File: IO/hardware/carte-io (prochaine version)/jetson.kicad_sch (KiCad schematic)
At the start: 8 parts, among them J1 Multiplex MPX 6, J23 Conn_02x20_Odd_Even, J26 114020164

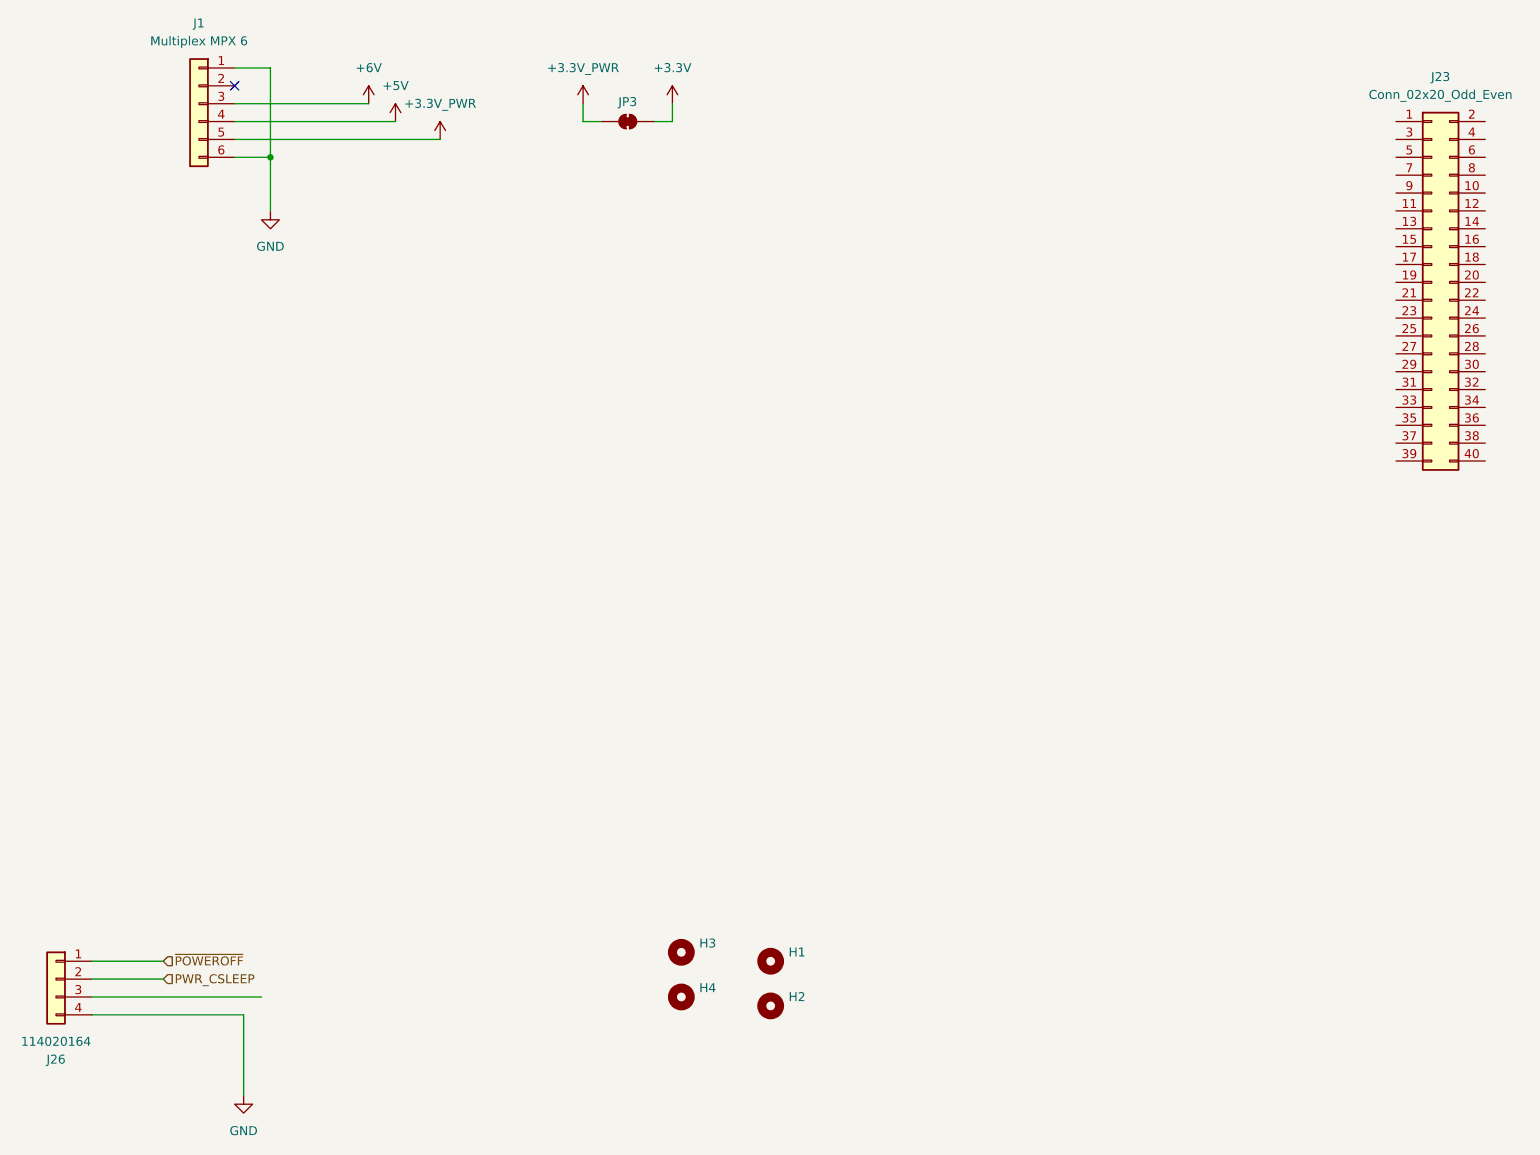
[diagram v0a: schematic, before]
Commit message: Recuperation de la carte IO perdue lors de la suppression des 3 derniers commit
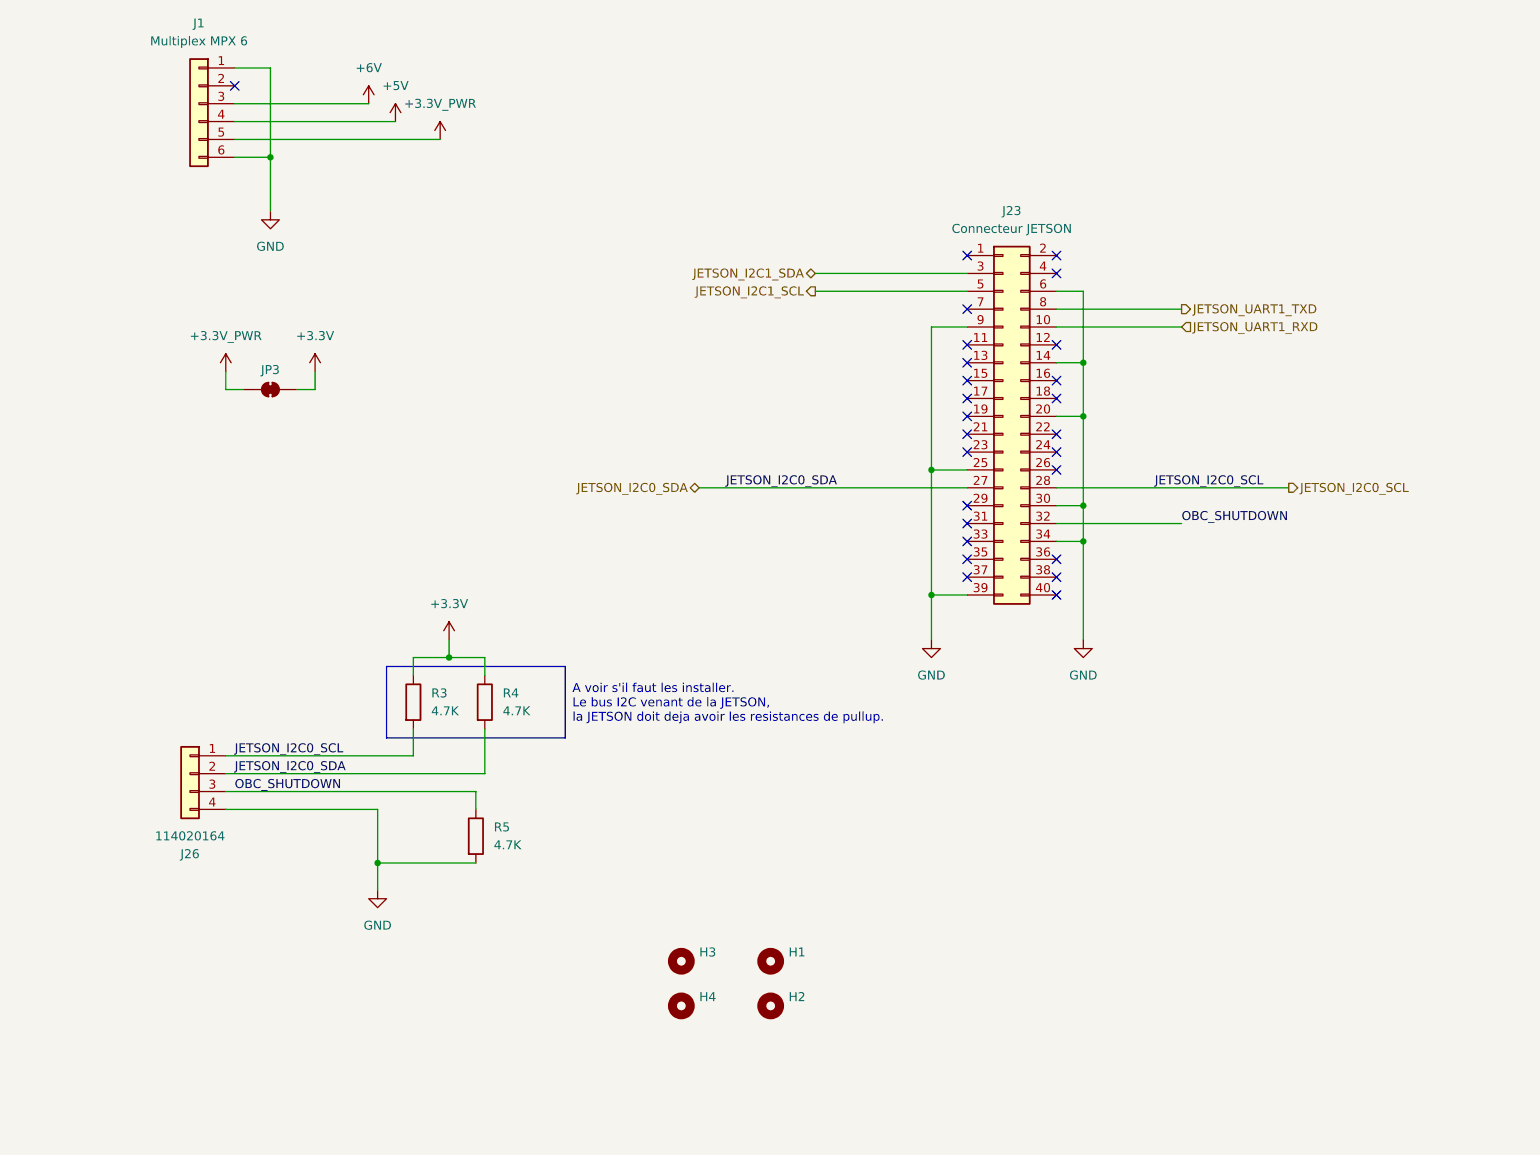
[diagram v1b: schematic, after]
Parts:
- added R3, R4, R5: 4.7K, Resistor_SMD:R_0805_2012Metric_Pad1.20x1.40mm_HandSolder, symbol Device:R
- J23: value Conn_02x20_Odd_Even -> Connecteur JETSON
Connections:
- net PWR_CSLEEP is gone; now on net JETSON_I2C0_SDA: J26.2 (Pin_2)
- net ~{POWEROFF} is gone; now on net JETSON_I2C0_SCL: J26.1 (Pin_1)
- net +3.3V: now also R3.1, R4.1
- net GND: now also J23.14 (Pin_14), J23.20 (Pin_20), J23.25 (Pin_25), J23.30 (Pin_30), J23.34 (Pin_34), J23.39 (Pin_39), J23.6 (Pin_6), J23.9 (Pin_9), R5.2
- net OBC_SHUTDOWN: now reaches J26.3 (Pin_3)
- net OBC_SHUTDOWN: now also J23.32 (Pin_32), R5.1
- net JETSON_UART1_RXD: now reaches J23.10 (Pin_10)
- net JETSON_I2C0_SDA: now reaches J23.27 (Pin_27)
- net JETSON_I2C0_SDA: now also R4.2
- net JETSON_I2C0_SCL: now reaches J23.28 (Pin_28)
- net JETSON_I2C0_SCL: now also R3.2
- net JETSON_I2C1_SDA: now reaches J23.3 (Pin_3)
- net JETSON_I2C1_SCL: now reaches J23.5 (Pin_5)
- net JETSON_UART1_TXD: now reaches J23.8 (Pin_8)
- no-connect marks 1 -> 26
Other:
- note added: "A voir s'il faut les installer. Le bus I2C venant de la JETSON, la JETSON doit deja avoir les resistances de pullup."
- title: Puissance -> Jetson-Alimentation
- moved on the sheet: H3, H4, J23, J26, JP3
